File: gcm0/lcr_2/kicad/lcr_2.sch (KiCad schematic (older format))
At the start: 128 parts, among them J1 5V, J2 -5V, J3 Conn_01x01_Male, J4 Conn_01x03_Male, J5 Conn_01x01_Male, J6 Conn_01x01_Male, J8 SWD, Q1 BC547, Q2 BC547, Q3 BC547, SW1 1, SW2 2, U1 RC4580, U10 RC4580, U11 74HC595, U12 STM32F030F4P6, U2 74HC4053PW,112, U3 74HC4052PW,118, U4 RC4580, U5 LM2596S-5, U6 LM7805_TO220, U7 RC4580, U8 LM1117-3.3, U9 74HC4053PW,112, Y1 8M

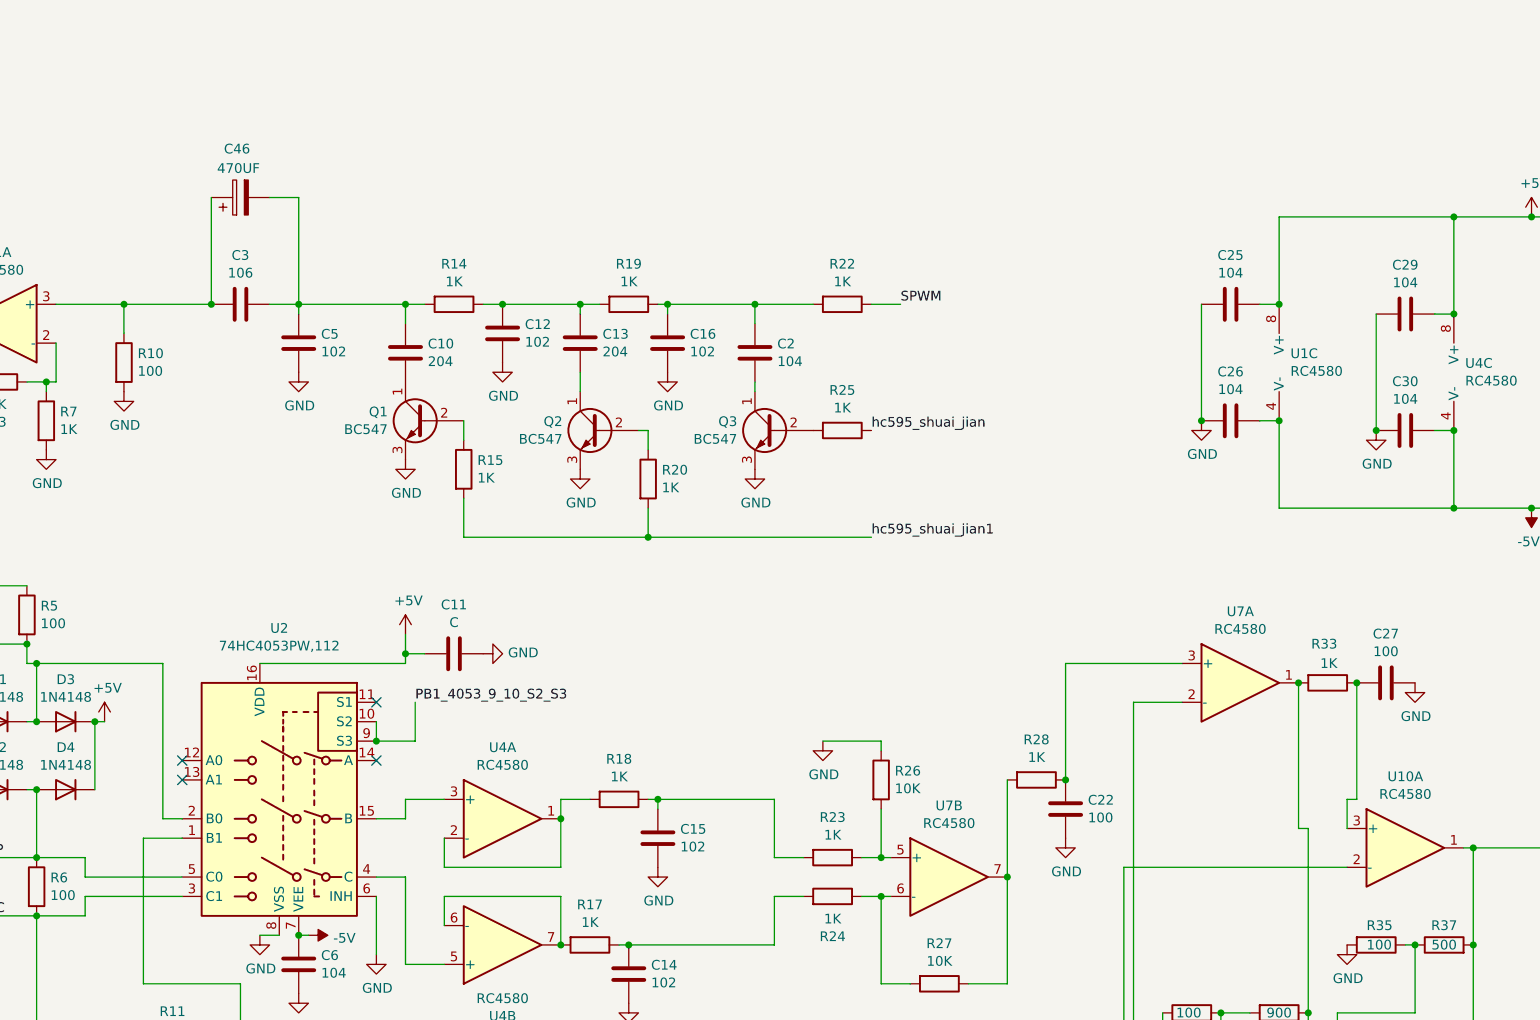
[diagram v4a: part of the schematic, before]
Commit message: 修改上下臂切换程序
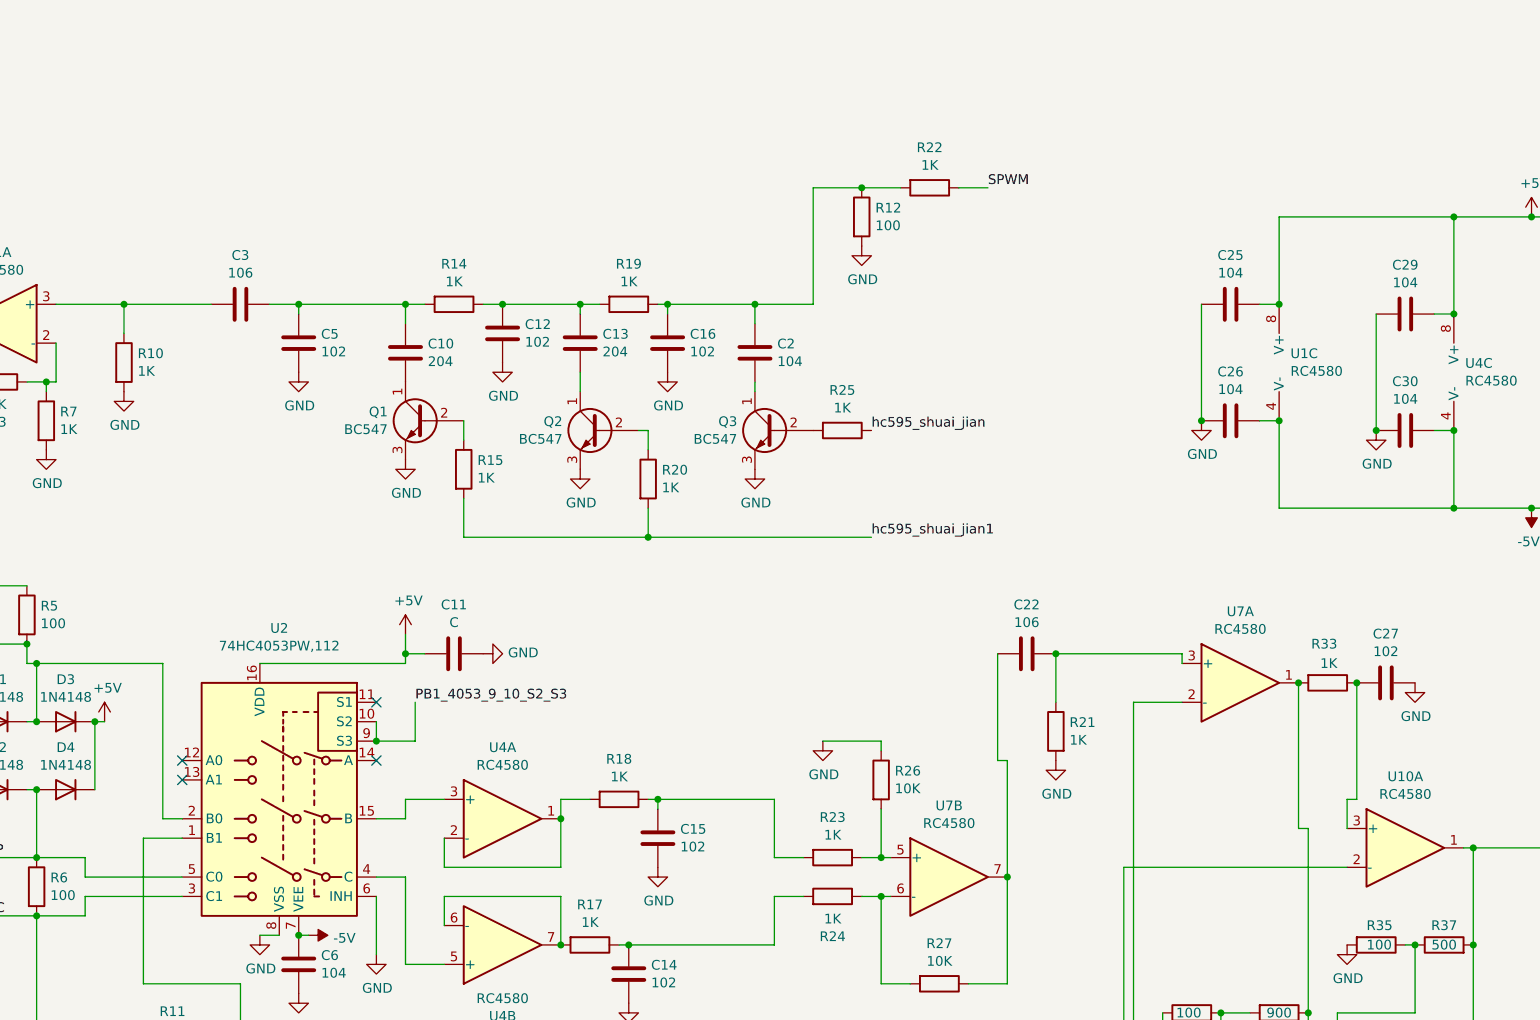
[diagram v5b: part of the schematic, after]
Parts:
- removed C46: 470UF, Capacitor_THT:CP_Radial_D8.0mm_P3.80mm, symbol Device:CP
- removed R28: 1K, Resistor_THT:R_Axial_DIN0204_L3.6mm_D1.6mm_P1.90mm_Vertical, symbol Device:R
- added R12: 100, symbol Device:R
- added R21: 1K, symbol Device:R
- C22: value 100 -> 106; footprint Capacitor_SMD:C_0603_1608Metric_Pad1.08x0.95mm_HandSolder -> (none)
- C27: value 100 -> 102
- R10: value 100 -> 1K
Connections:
- net GND: now also R12.2, R21.2; no longer C22.2
- net at C16.1, C2.1, R19.1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: now also R12.1
- net at C22.1, U7.3 (+): now also R21.1
- net at R27.1, U7.7: now also C22.2
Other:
- moved on the sheet: R22
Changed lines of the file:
@@
 	3500 2750 4450 2750
 Connection ~ 4450 2750
-Text Label 5750 1550 0    50   ~ 0
+Text Label 6200 950  0    50   ~ 0
 SPWM
 $Comp
@@
 L Device:R R22
 U 1 1 625D8345
-P 5450 1550
-F 0 "R22" V 5243 1550 50  0000 C CNN
-F 1 "1K" V 5334 1550 50  0000 C CNN
-F 2 "Resistor_THT:R_Axial_DIN0204_L3.6mm_D1.6mm_P1.90mm_Vertical" V 5380 1550 50  0001 C CNN
-F 3 "~" H 5450 1550 50  0001 C CNN
-	1    5450 1550
-	0    1    1    0
-$EndComp
-Wire Wire Line
-	5600 1550 5750 1550
+P 5900 950
+F 0 "R22" V 5693 950 50  0000 C CNN
+F 1 "1K" V 5784 950 50  0000 C CNN
+F 2 "Resistor_THT:R_Axial_DIN0204_L3.6mm_D1.6mm_P1.90mm_Vertical" V 5830 950 50  0001 C CNN
+F 3 "~" H 5900 950 50  0001 C CNN
+	1    5900 950
+	0    1    1    0
+$EndComp
+Wire Wire Line
+	6050 950  6200 950
 Wire Wire Line
 	3700 1550 4100 1550
@@
 P 1750 1850
 F 0 "R10" H 1820 1896 50  0000 L CNN
-F 1 "100" H 1820 1805 50  0000 L CNN
+F 1 "1K" H 1820 1805 50  0000 L CNN
 F 2 "Resistor_THT:R_Axial_DIN0204_L3.6mm_D1.6mm_P1.90mm_Vertical" V 1680 1850 50  0001 C CNN
 F 3 "~" H 1750 1850 50  0001 C CNN
@@
 Wire Wire Line
 	6300 4500 6300 5050
-Wire Wire Line
-	6300 4000 6300 4500
-Connection ~ 6300 4500
 $Comp
 L power:+5V #PWR045
@@
 D\nU\nT
 $Comp
-L Device:R R28
-U 1 1 631C384C
-P 6450 4000
-F 0 "R28" V 6243 4000 50  0000 C CNN
-F 1 "1K" V 6334 4000 50  0000 C CNN
-F 2 "Resistor_THT:R_Axial_DIN0204_L3.6mm_D1.6mm_P1.90mm_Vertical" V 6380 4000 50  0001 C CNN
-F 3 "~" H 6450 4000 50  0001 C CNN
-	1    6450 4000
-	0    1    1    0
-$EndComp
-Wire Wire Line
-	7200 3400 6600 3400
-Wire Wire Line
-	6950 3600 6950 6700
-Wire Wire Line
-	6600 3400 6600 4000
-$Comp
 L Device:C C27
 U 1 1 632A707B
 P 8250 3500
 F 0 "C27" V 7998 3500 50  0000 C CNN
-F 1 "100" V 8089 3500 50  0000 C CNN
+F 1 "102" V 8089 3500 50  0000 C CNN
 F 2 "Capacitor_SMD:C_0603_1608Metric_Pad1.08x0.95mm_HandSolder" H 8288 3350 50  0001 C CNN
 F 3 "~" H 8250 3500 50  0001 C CNN
@@
 L power:GND #PWR035
 U 1 1 631C7937
-P 6600 4300
-F 0 "#PWR035" H 6600 4050 50  0001 C CNN
-F 1 "GND" H 6605 4127 50  0000 C CNN
-F 2 "" H 6600 4300 50  0001 C CNN
-F 3 "" H 6600 4300 50  0001 C CNN
-	1    6600 4300
-	1    0    0    -1
-$EndComp
-$Comp
-L Device:C C22
-U 1 1 631C5B0A
-P 6600 4150
-F 0 "C22" H 6715 4196 50  0000 L CNN
-F 1 "100" H 6715 4105 50  0000 L CNN
-F 2 "Capacitor_SMD:C_0603_1608Metric_Pad1.08x0.95mm_HandSolder" H 6638 4000 50  0001 C CNN
-F 3 "~" H 6600 4150 50  0001 C CNN
-	1    6600 4150
+P 6550 3900
+F 0 "#PWR035" H 6550 3650 50  0001 C CNN
+F 1 "GND" H 6555 3727 50  0000 C CNN
+F 2 "" H 6550 3900 50  0001 C CNN
+F 3 "" H 6550 3900 50  0001 C CNN
+	1    6550 3900
 	1    0    0    -1
 $EndComp
@@
 	0    1    1    0
 $EndComp
-Connection ~ 6600 4000
 Text Notes 10350 3200 0    50   ~ 0
 3_bei
@@
 	5300 1550 5000 1550
 Connection ~ 5000 1550
-$Comp
-L Device:CP C46
-U 1 1 620E9A56
-P 2350 1000
-F 0 "C46" V 2600 950 50  0000 L CNN
-F 1 "470UF" V 2500 900 50  0000 L CNN
-F 2 "Capacitor_THT:CP_Radial_D8.0mm_P3.80mm" H 2388 850 50  0001 C CNN
-F 3 "~" H 2350 1000 50  0001 C CNN
-	1    2350 1000
-	0    -1   -1   0
-$EndComp
-Wire Wire Line
-	2500 1000 2650 1000
-Wire Wire Line
-	2650 1000 2650 1550
-Wire Wire Line
-	2200 1000 2200 1550
-Connection ~ 2200 1550
 Connection ~ 2650 5700
 Wire Wire Line
@@
 	3400 6100 3400 6200
 Connection ~ 3400 6200
+$Comp
+L Device:C C22
+U 1 1 61EF0995
+P 6400 3350
+F 0 "C22" V 6148 3350 50  0000 C CNN
+F 1 "106" V 6239 3350 50  0000 C CNN
+F 2 "" H 6438 3200 50  0001 C CNN
+F 3 "~" H 6400 3350 50  0001 C CNN
+	1    6400 3350
+	0    1    1    0
+$EndComp
+$Comp
+L Device:R R21
+U 1 1 61F2F8E4
+P 6550 3750
+F 0 "R21" H 6480 3796 50  0000 R CNN
+F 1 "1K" H 6480 3705 50  0000 R CNN
+F 2 "" V 6480 3750 50  0001 C CNN
+F 3 "~" H 6550 3750 50  0001 C CNN
+	1    6550 3750
+	-1   0    0    -1
+$EndComp
+Wire Wire Line
+	5750 950  5550 950
+Wire Wire Line
+	5300 950  5300 1550
+$Comp
+L Device:R R12
+U 1 1 621239DC
+P 5550 1100
+F 0 "R12" H 5620 1146 50  0000 L CNN
+F 1 "100" H 5620 1055 50  0000 L CNN
+F 2 "" V 5480 1100 50  0001 C CNN
+F 3 "~" H 5550 1100 50  0001 C CNN
+	1    5550 1100
+	1    0    0    -1
+$EndComp
+Connection ~ 5550 950
+Wire Wire Line
+	5550 950  5300 950
+$Comp
+L power:GND #PWR09
+U 1 1 621257B8
+P 5550 1250
+F 0 "#PWR09" H 5550 1000 50  0001 C CNN
+F 1 "GND" H 5555 1077 50  0000 C CNN
+F 2 "" H 5550 1250 50  0001 C CNN
+F 3 "" H 5550 1250 50  0001 C CNN
+	1    5550 1250
+	1    0    0    -1
+$EndComp
+Wire Wire Line
+	6950 3600 6950 6700
+Wire Wire Line
+	6550 3350 7200 3350
+Wire Wire Line
+	7200 3350 7200 3400
+Wire Wire Line
+	6250 3350 6250 3900
+Wire Wire Line
+	6250 3900 6300 3900
+Wire Wire Line
+	6300 3900 6300 4500
+Connection ~ 6300 4500
+Wire Wire Line
+	6550 3600 6550 3350
+Connection ~ 6550 3350
 $EndSCHEMATC

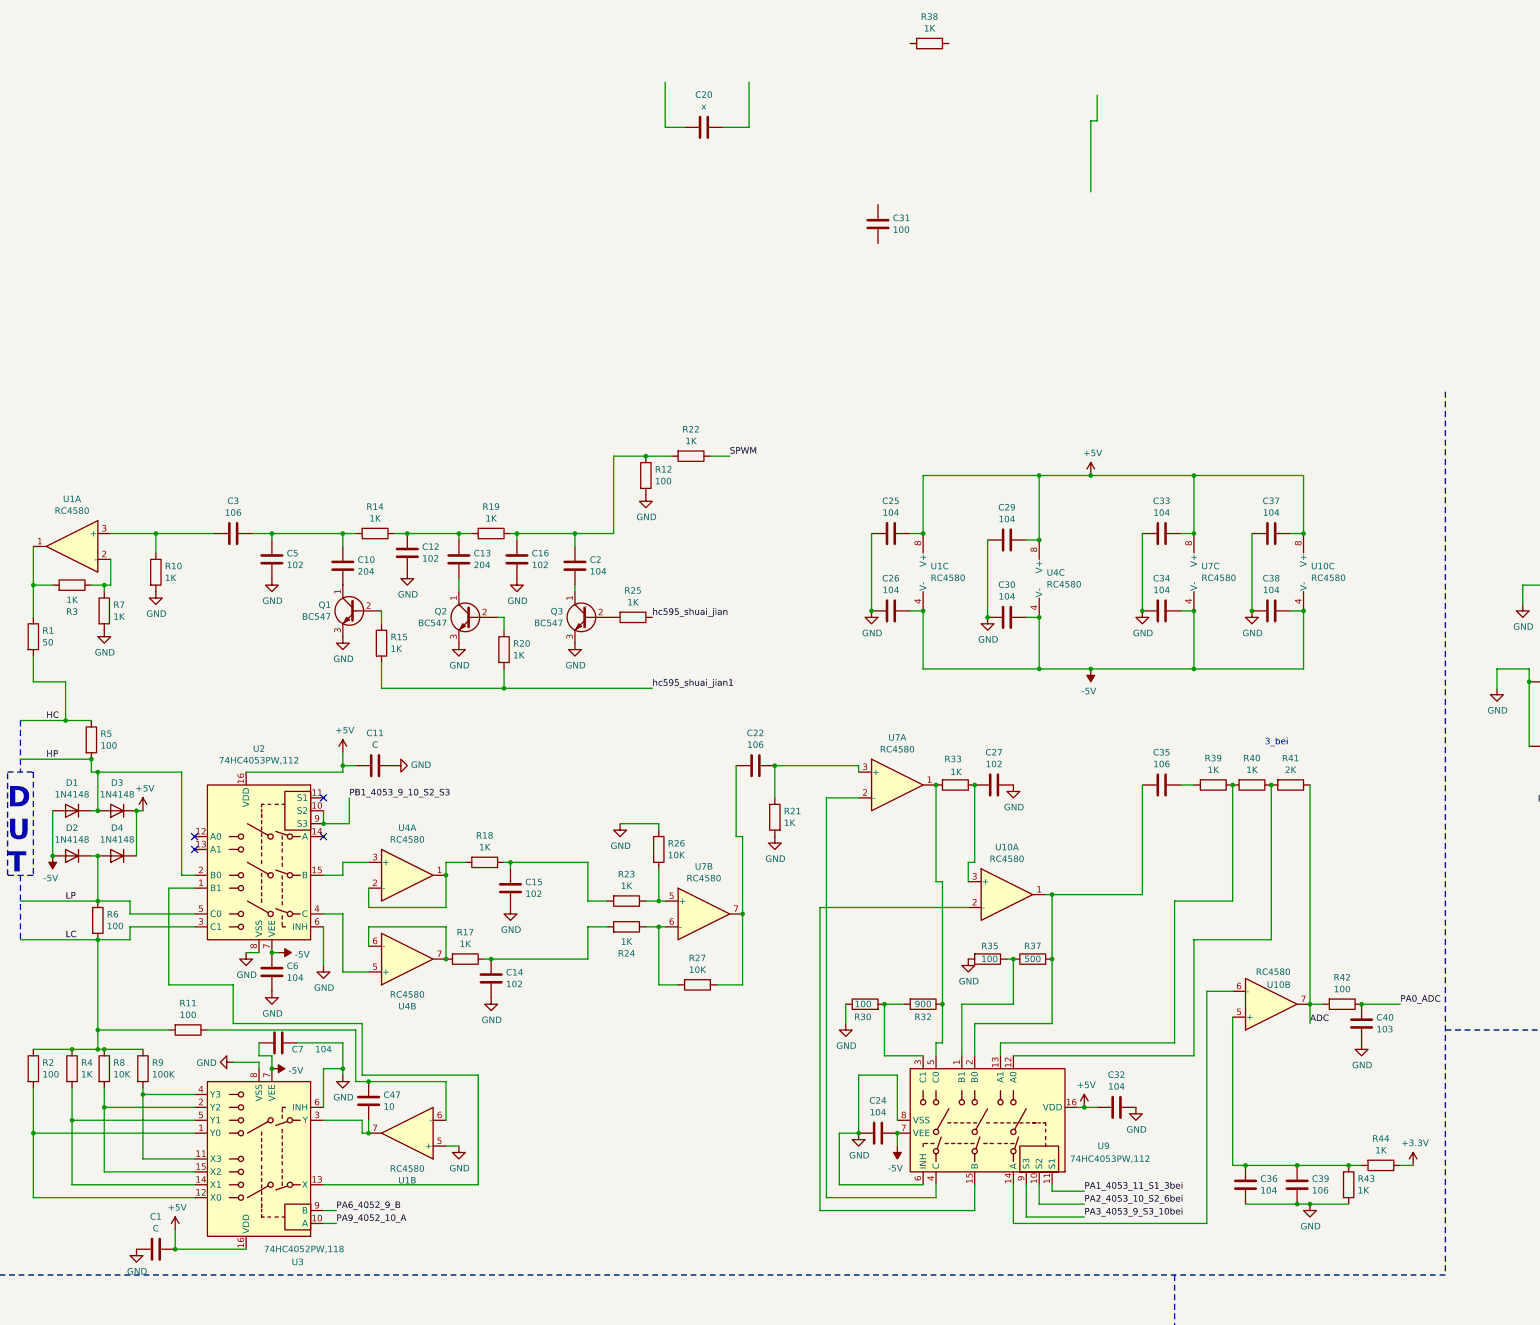
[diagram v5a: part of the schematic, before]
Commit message: 修改采样率
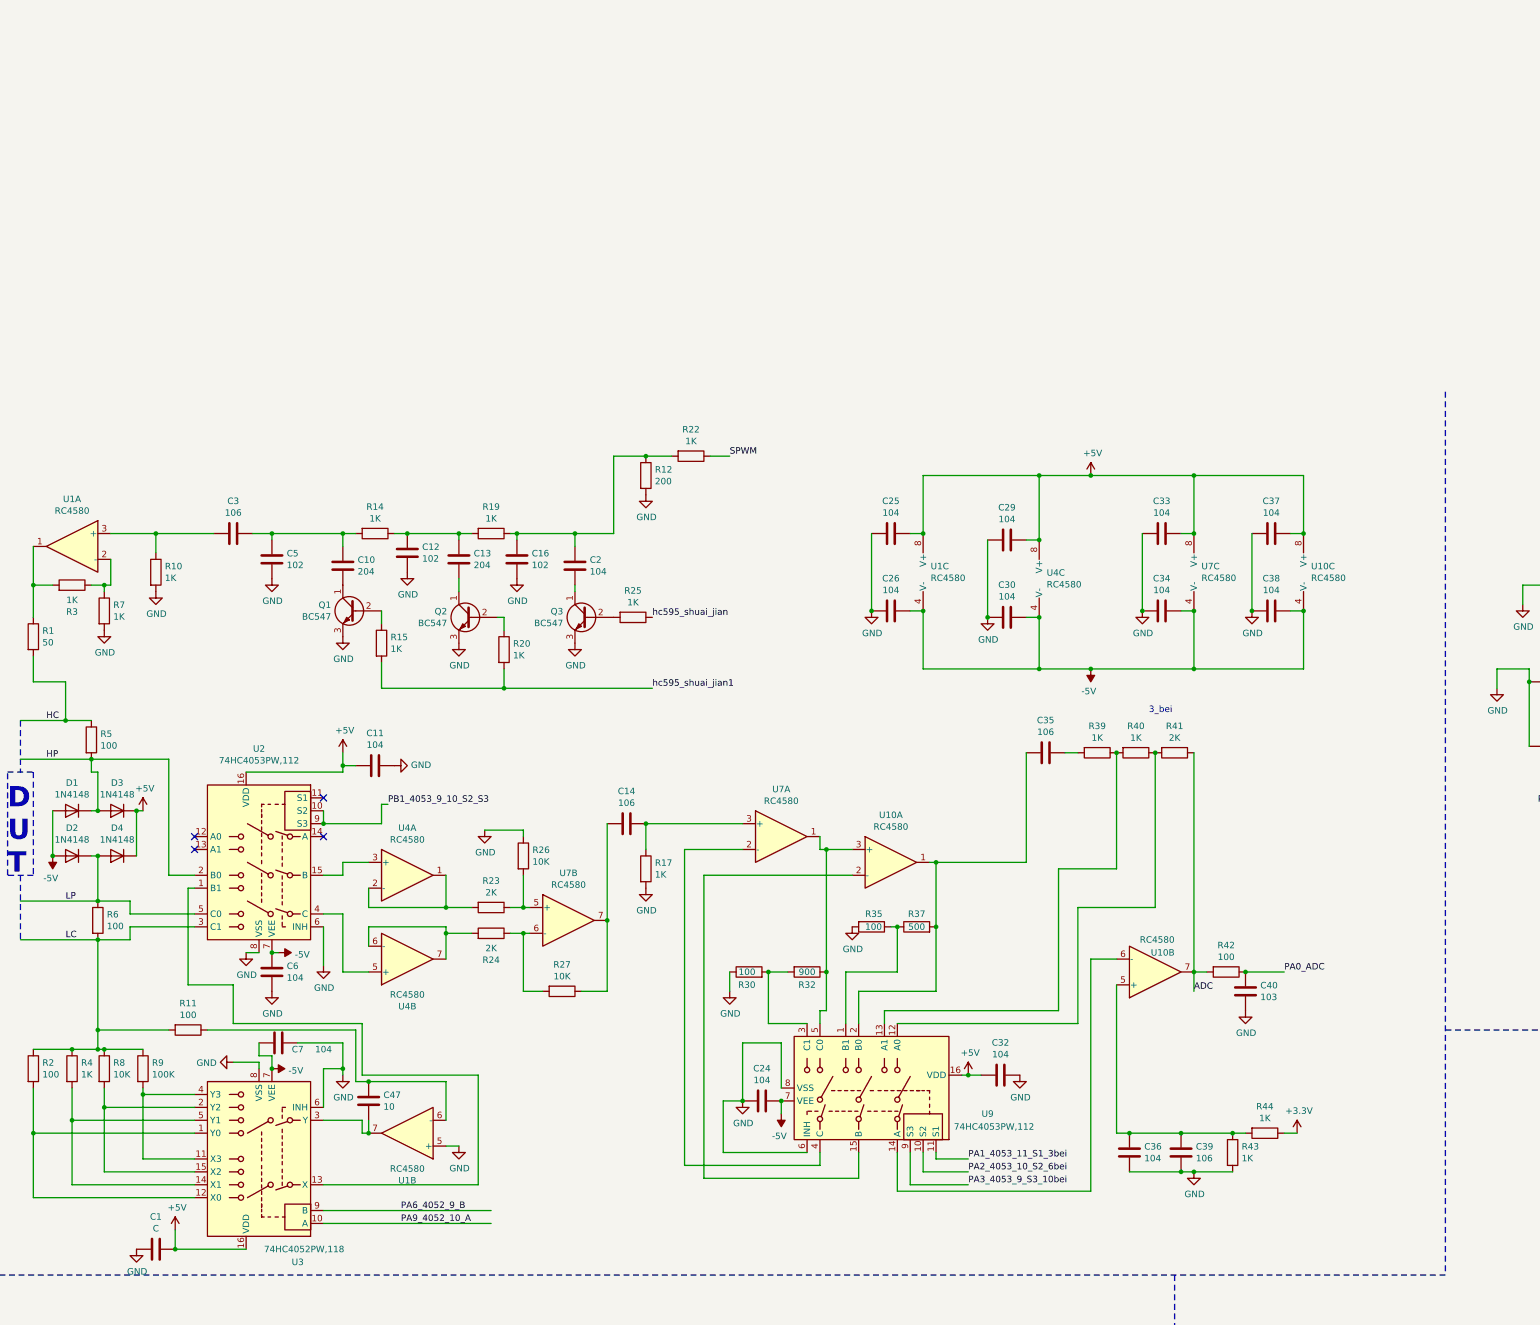
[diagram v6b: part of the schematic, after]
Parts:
- removed C15, C27: 102, Capacitor_SMD:C_0603_1608Metric_Pad1.08x0.95mm_HandSolder, symbol Device:C
- removed C20: x, Capacitor_SMD:C_0603_1608Metric_Pad1.08x0.95mm_HandSolder, symbol Device:C
- removed C22: 106, symbol Device:C
- removed C31: 100, Capacitor_SMD:C_0603_1608Metric_Pad1.08x0.95mm_HandSolder, symbol Device:C
- removed R18, R33, R38: 1K, Resistor_THT:R_Axial_DIN0204_L3.6mm_D1.6mm_P1.90mm_Vertical, symbol Device:R
- removed R21: 1K, symbol Device:R
- C11: value C -> 104
- C14: value 102 -> 106; footprint Capacitor_SMD:C_0603_1608Metric_Pad1.08x0.95mm_HandSolder -> Capacitor_SMD:C_0805_2012Metric_Pad1.18x1.45mm_HandSolder
- C47: footprint (none) -> Capacitor_SMD:C_0603_1608Metric_Pad1.08x0.95mm_HandSolder
- R12: value 100 -> 200; footprint (none) -> Resistor_THT:R_Axial_DIN0204_L3.6mm_D1.6mm_P1.90mm_Vertical
- R23, R24: value 1K -> 2K
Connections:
- net GND: now also R17.2; no longer C14.2
- net at U4.1, U4.2 (-): now also R23.2
- net at U4.6 (-), U4.7: now also R24.2; no longer R17.2
- net at R32.1, U7.1, U9.5 (C0): now also U10.3 (+)
- net at U7.3 (+): now also C14.1, R17.1
- net at R27.1, U7.7: now also C14.2
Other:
- moved on the sheet: C24, C32, C35, C36, C39, C40, R23, R24, R26, R27, R30, R32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
